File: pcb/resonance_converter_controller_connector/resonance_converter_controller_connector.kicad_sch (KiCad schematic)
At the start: 33 parts, among them J1 Conn_01x02, J10 Conn_01x04, J11 Conn_01x04, J12 Conn_01x02, J13 Conn_01x06, J14 Conn_02x05_Odd_Even, J15 Conn_01x02, J16 Conn_01x02, J17 Conn_01x02, J18 Conn_01x08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

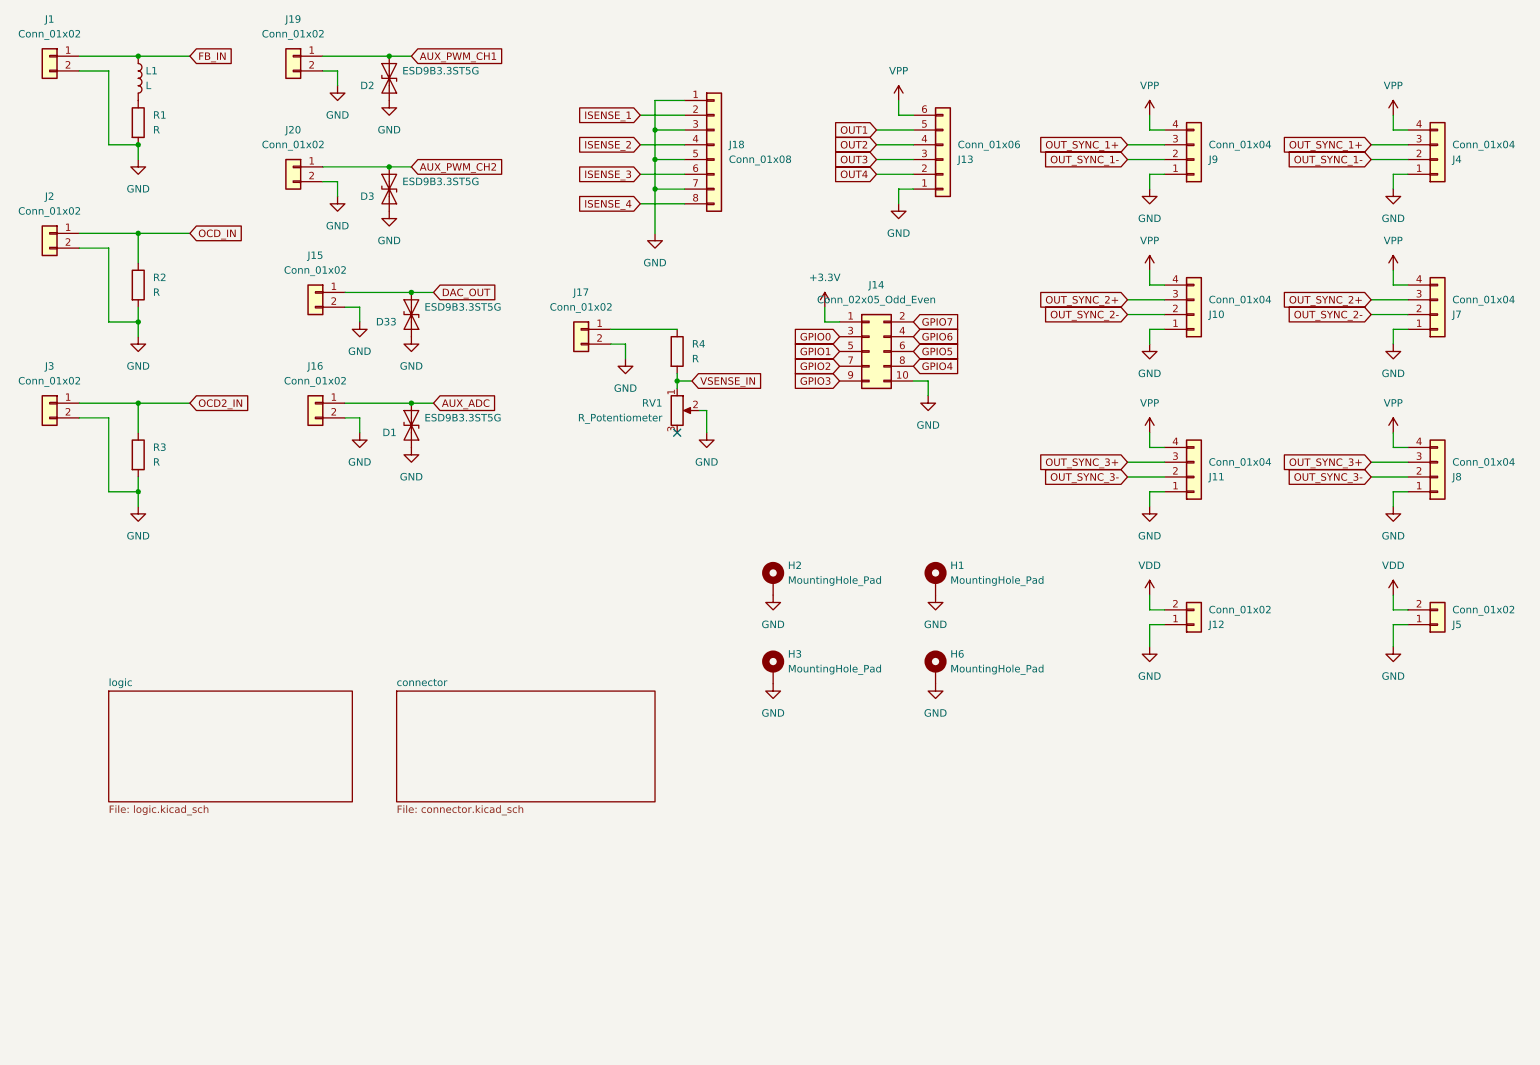
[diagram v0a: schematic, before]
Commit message: Add 3rd row of output connectors
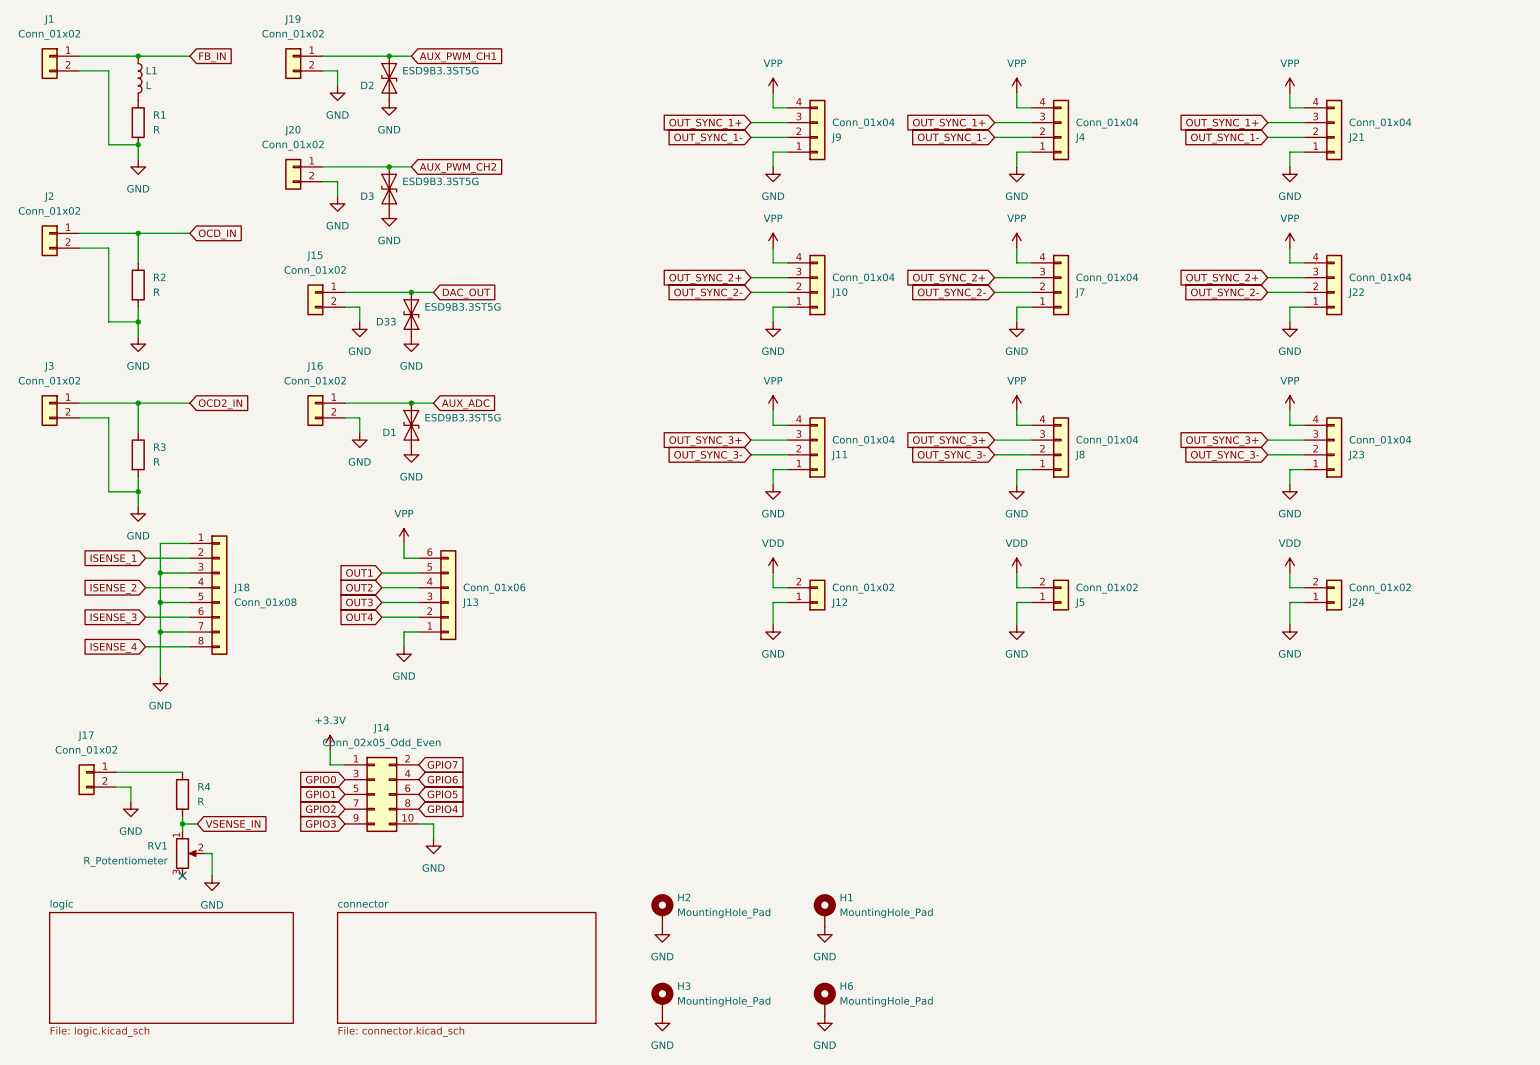
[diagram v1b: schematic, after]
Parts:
- added J21, J22, J23: Conn_01x04, Connector_JST:JST_PH_B4B-PH-K_1x04_P2.00mm_Vertical, symbol Connector_Generic:Conn_01x04
- added J24: Conn_01x02, Connector_AMASS:AMASS_XT30U-M_1x02_P5.0mm_Vertical, symbol Connector_Generic:Conn_01x02
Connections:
- net GND: now also J21.1 (Pin_1), J22.1 (Pin_1), J23.1 (Pin_1), J24.1 (Pin_1)
- net OUT_SYNC_1+: now also J21.3 (Pin_3)
- net OUT_SYNC_1-: now also J21.2 (Pin_2)
- net OUT_SYNC_2+: now also J22.3 (Pin_3)
- net OUT_SYNC_2-: now also J22.2 (Pin_2)
- net OUT_SYNC_3+: now also J23.3 (Pin_3)
- net OUT_SYNC_3-: now also J23.2 (Pin_2)
- net VDD: now also J24.2 (Pin_2)
- net VPP: now also J21.4 (Pin_4), J22.4 (Pin_4), J23.4 (Pin_4)
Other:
- moved on the sheet: H1, H2, H3, H6, J10, J11, J12, J13, J14, J17, J18, J4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
